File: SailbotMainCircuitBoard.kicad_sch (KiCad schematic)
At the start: 23 parts, among them IC1 BQ7790400PWR, J1 B5B-XH-A, Q1 BSS138, Q2 BSS138

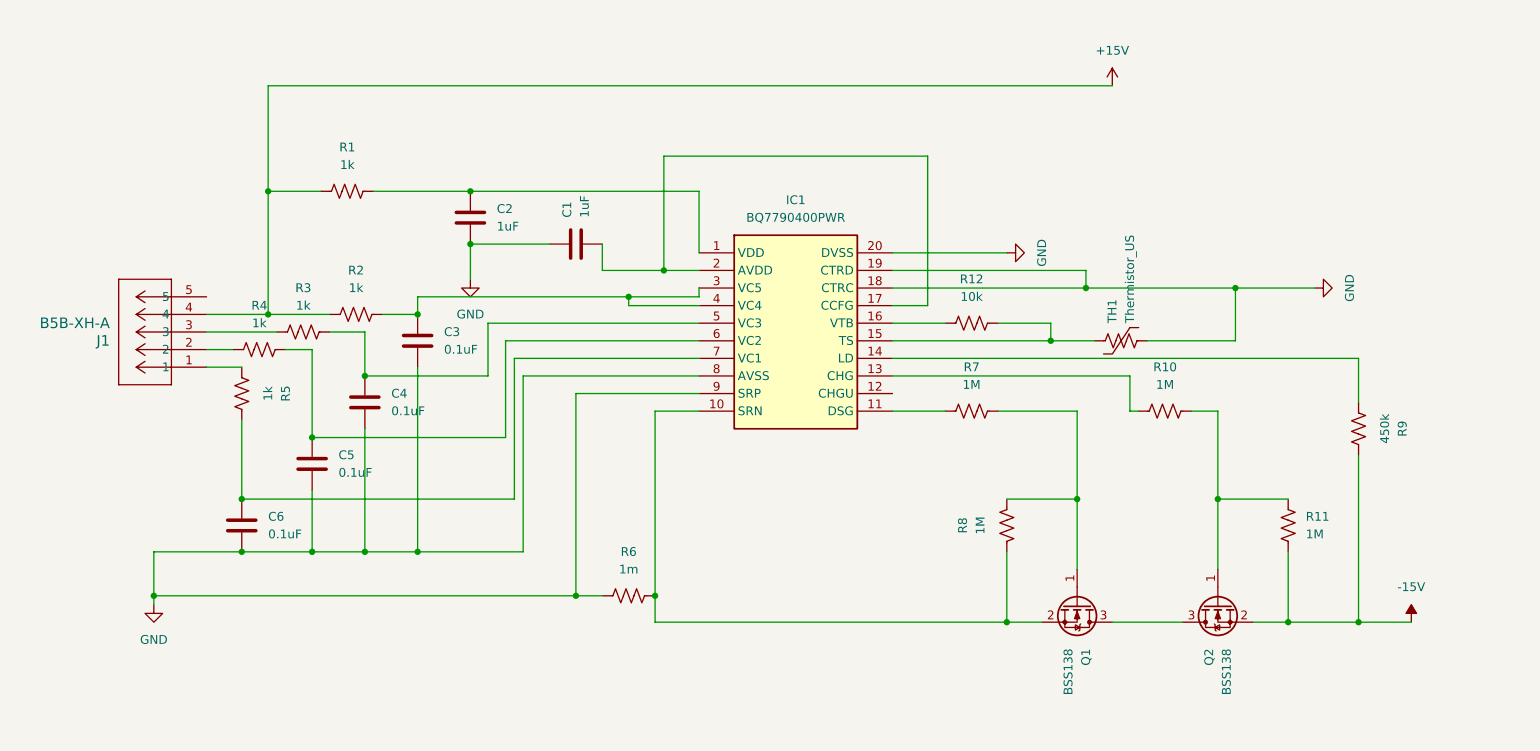
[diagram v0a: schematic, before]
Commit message: Added ADC Circuit schetch to read individual cell voltages
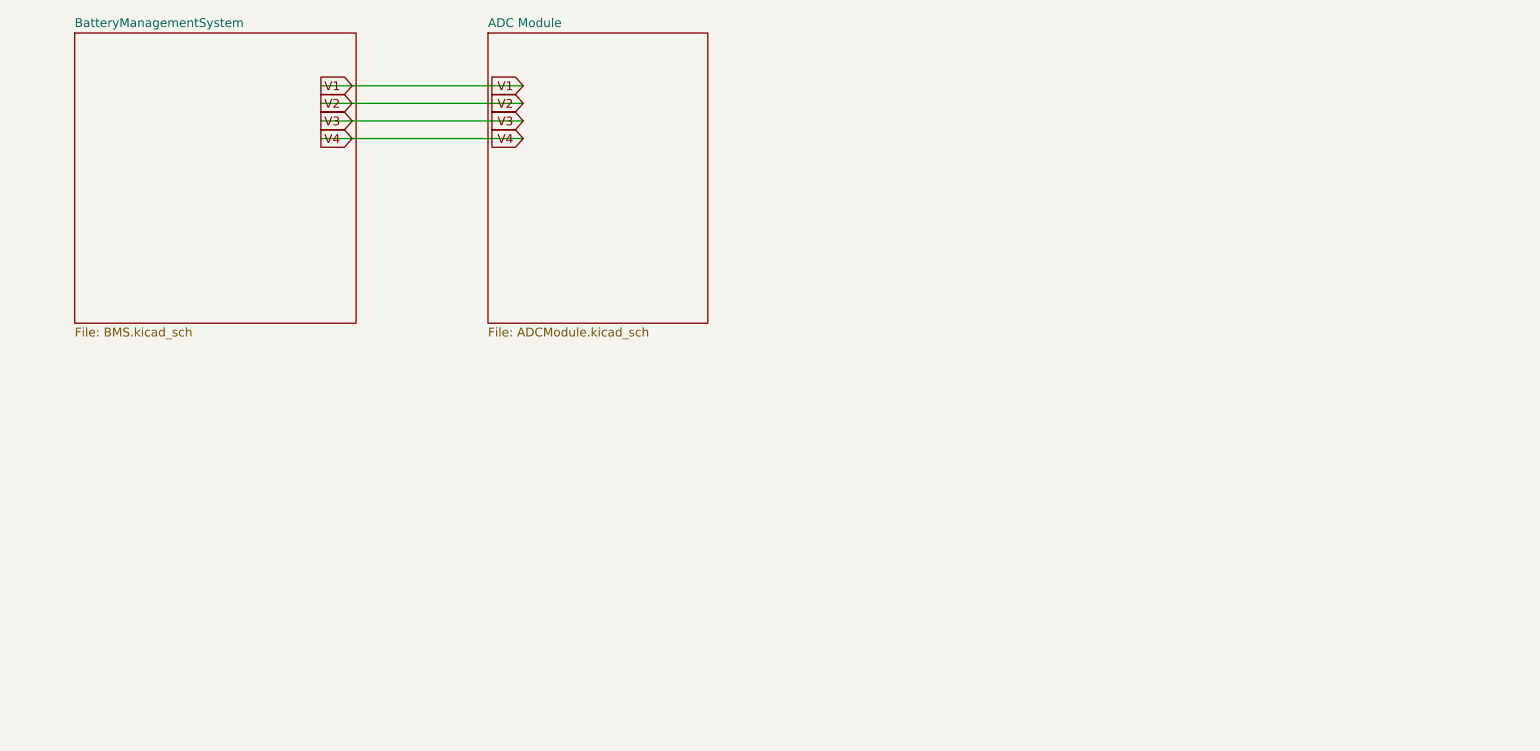
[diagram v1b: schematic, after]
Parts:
- removed C1, C2: 1uF, symbol Device:C
- removed C3, C4, C5, C6: 0.1uF, symbol Device:C
- removed IC1: BQ7790400PWR, SOP65P640X120-20N, symbol BQ7790400PWR:BQ7790400PWR
- removed J1: B5B-XH-A, CONN_B5B-XH-A_JST, symbol B5B-XH-A:B5B-XH-A
- removed Q1, Q2: BSS138, Package_TO_SOT_SMD:SOT-23, symbol Transistor_FET:BSS138
- removed R1, R2, R3, R4, R5: 1k, symbol Device:R_US
- removed R10, R11, R7, R8: 1M, symbol Device:R_US
- removed R12: 10k, symbol Device:R_US
- removed R6: 1m, symbol Device:R_US
- removed R9: 450k, symbol Device:R_US
- removed TH1: Thermistor_US, symbol Device:Thermistor_US
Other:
- added sheet ADC Module (ADCModule.kicad_sch)
- added sheet BatteryManagementSystem (BMS.kicad_sch)

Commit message: Pushing updated schematics
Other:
- added sheet 5VConverter (5VConverter.kicad_sch)
- added sheet ADC_Module2 (ADC_Module2.kicad_sch)
- added sheet ESP32 Coprocessor (ESP32_Coprocessor.kicad_sch)
- added sheet JetsonOrinNano (JetsonOrinNano.kicad_sch)
- note added: "Main 5V Output"
